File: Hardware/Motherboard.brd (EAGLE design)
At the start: 124.5 x 73.7 mm, 99 parts, among them J1 MICROMOD-2222-C, J10 MICRO-SD-PUSH-PUSH-EXT-PIN, J2 Vertical Qwiic Connector, J4 QWIIC_RIGHT_ANGLE, J5 CORTEX_JTAG_DEBUG_MINIMUM_PTH, J6 MICROMOD_CARRIER, J7 MICROMOD_CARRIER, Q1 3.1A/30V/105mΩ, U2 MCP73831, U5 AP7361C-33

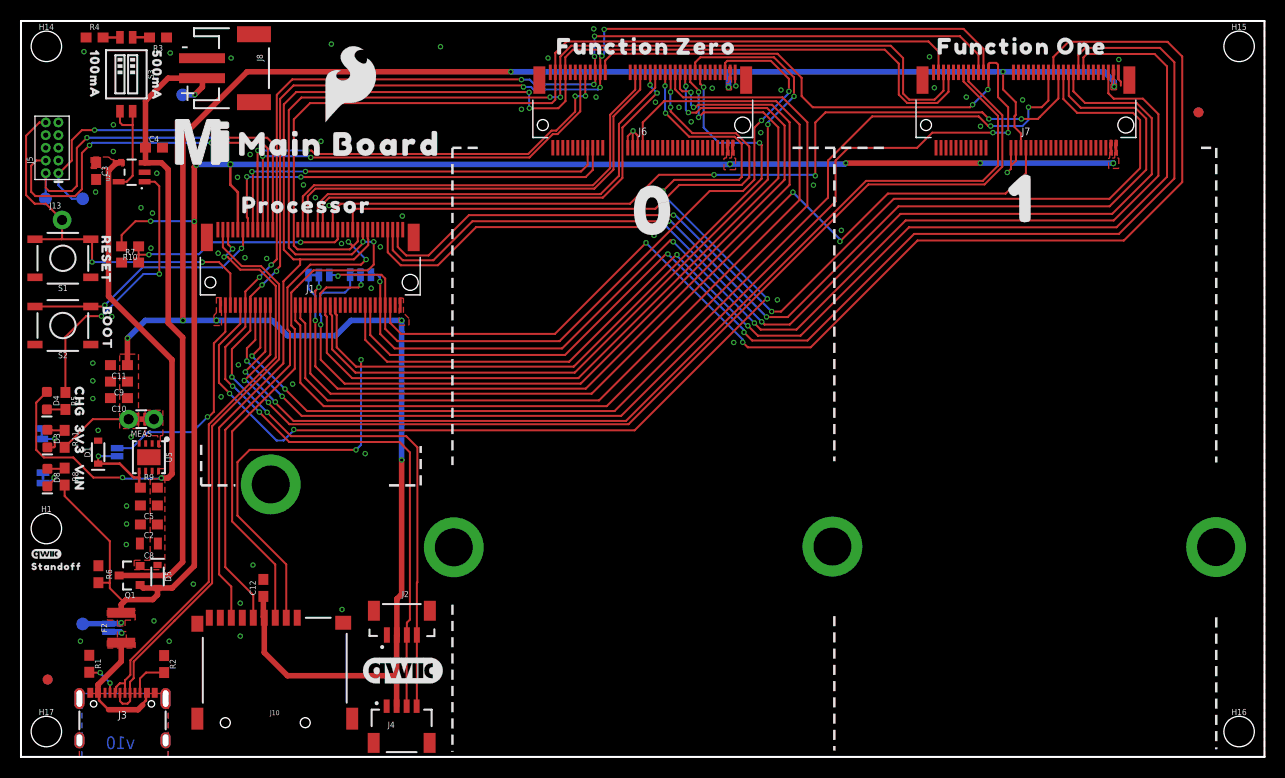
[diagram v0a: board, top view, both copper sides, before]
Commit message: Adds PTH headers for shunt selectable settings on G0 and G1 for PWR_EN0 and PWR_EN1 respectively
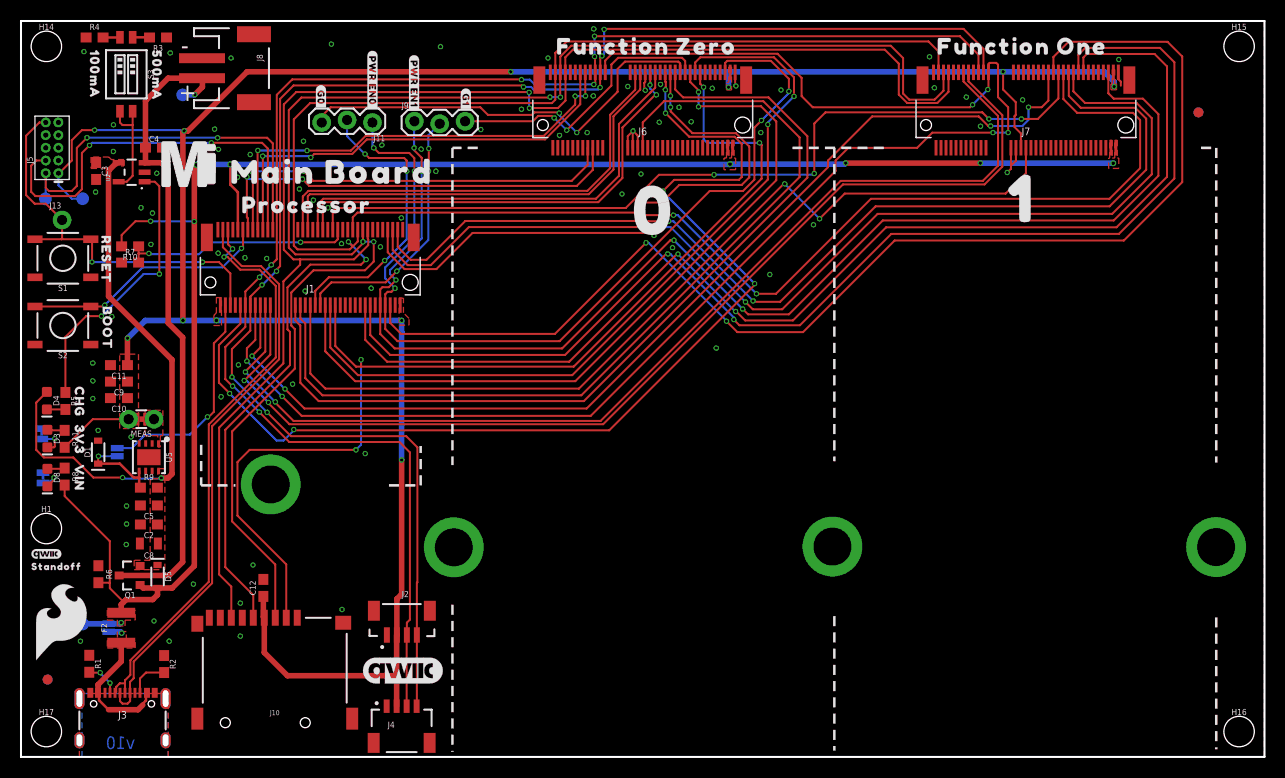
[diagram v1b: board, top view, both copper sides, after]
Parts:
- removed JP1, JP2: JUMPER-SMT_3_1-NC_TRACE_SILK, SparkFun-Jumpers:SMT-JUMPER_3_1-NC_TRACE_SILK
- removed U$28: (no value), top:#ALT_PWR_EN0#517
- added J11, J9: (no value), SparkFun-Connectors:1X03_LOCK
- added U$29: (no value), top:#PWR_EN0#517
- U$25: device top:#G1#PROCESSOR#517 -> top:#PWR_EN1#517
- U$26: device top:#G0#PROCESSOR#517 -> top:#G0#517
- U$27: device top:#ALT_PWR_EN1#517 -> top:#G1#517
- moved U$24 61.1 mm to (4.06, 13.5)
- moved U$25 25.3 mm to (39.3, 67.4), flipped to the top, turned to 270 degrees
- moved U$27 24.4 mm to (44.5, 65.8), flipped to the top, turned to 270 degrees
- moved U$26 23.4 mm to (30.0, 66.0), flipped to the top, turned to 270 degrees
- moved U$21 2.90 mm to (31.1, 58.5)
- moved U$14 2.61 mm to (16.8, 59.4)
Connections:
- net G0-JUMPER: now also J11.2; no longer JP2.2
- net G0-PROCESSOR: now also J11.3; no longer JP2.3
- net G1-JUMPER: now also J9.2; no longer JP1.2
- net G1-PROCESSOR: now also J9.3; no longer JP1.3
- net PWR_EN0: now also J11.1; no longer JP2.1
- net PWR_EN1: now also J9.1; no longer JP1.1
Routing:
- net G1-PROCESSOR: track 87.1 -> 28.4 mm, vias 3 -> 2
- net G0-PROCESSOR: track 87.9 -> 43.5 mm, vias 3 -> 2
- net G0-JUMPER: track 3.16 -> 29.2 mm, vias 1 -> 3
- net G1-JUMPER: track 6.64 -> 26.3 mm, vias 1 -> 3
- net PWR_EN1: track 113.9 -> 130.1 mm, vias 3 -> 5
- net PWR_EN0: track 74.7 -> 90.3 mm, vias 3 -> 5
- net PWM0-PROCESSOR: track 92.7 -> 89.8 mm
- net D0-PROCESSOR: track 111.8 -> 109.3 mm
- net A0-PROCESSOR: track 93.9 -> 91.3 mm
- net D1-PROCESSOR: track 106.9 -> 104.9 mm
- net GND: track 13.0 -> 14.8 mm, vias 73 -> 86
- net I2C_!INT!: track 153.2 -> 151.5 mm
- net A1-PROCESSOR: track 95.2 -> 93.5 mm
- net !CS1!-PROCESSOR: track 124.9 -> 123.5 mm
- net G8-PROCESSOR: track 122.8 -> 121.5 mm
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
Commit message: Revert "Adds PTH headers for shunt selectable settings on G0 and G1 for PWR_EN0 and PWR_EN1 respectively"
This reverts commit ddf80de5a278d55282677fb1bccc97569ea5aff3.
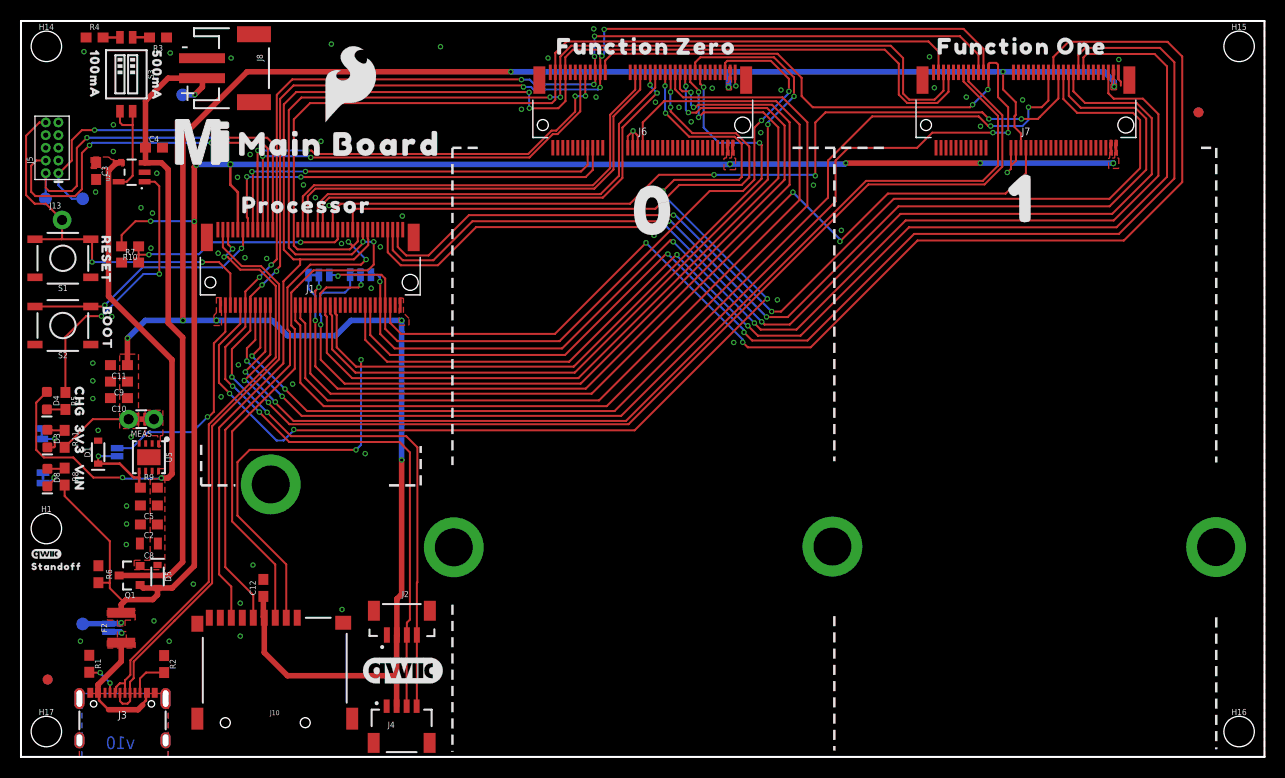
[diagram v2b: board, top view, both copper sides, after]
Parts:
- removed J11, J9: (no value), SparkFun-Connectors:1X03_LOCK
- removed U$29: (no value), top:#PWR_EN0#517
- added JP1, JP2: JUMPER-SMT_3_1-NC_TRACE_SILK, SparkFun-Jumpers:SMT-JUMPER_3_1-NC_TRACE_SILK
- added U$28: (no value), top:#ALT_PWR_EN0#517
- U$25: device top:#PWR_EN1#517 -> top:#G1#PROCESSOR#517
- U$26: device top:#G0#517 -> top:#G0#PROCESSOR#517
- U$27: device top:#G1#517 -> top:#ALT_PWR_EN1#517
- moved U$24 61.1 mm to (33.0, 67.3)
- moved U$25 25.3 mm to (33.4, 42.8), flipped to the bottom, turned to 90 degrees
- moved U$27 24.4 mm to (34.7, 43.4), flipped to the bottom, turned to 90 degrees
- moved U$26 23.4 mm to (29.2, 42.6), flipped to the bottom, turned to 90 degrees
- moved U$21 2.90 mm to (31.9, 61.3)
- moved U$14 2.61 mm to (18.2, 61.6)
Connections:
- net G0-JUMPER: now also JP2.2; no longer J11.2
- net G0-PROCESSOR: now also JP2.3; no longer J11.3
- net G1-JUMPER: now also JP1.2; no longer J9.2
- net G1-PROCESSOR: now also JP1.3; no longer J9.3
- net PWR_EN0: now also JP2.1; no longer J11.1
- net PWR_EN1: now also JP1.1; no longer J9.1
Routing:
- net G1-PROCESSOR: track 28.4 -> 87.1 mm, vias 2 -> 3
- net G0-PROCESSOR: track 43.5 -> 87.9 mm, vias 2 -> 3
- net G0-JUMPER: track 29.2 -> 3.16 mm, vias 3 -> 1
- net G1-JUMPER: track 26.3 -> 6.64 mm, vias 3 -> 1
- net PWR_EN1: track 130.1 -> 113.9 mm, vias 5 -> 3
- net PWR_EN0: track 90.3 -> 74.7 mm, vias 5 -> 3
- net PWM0-PROCESSOR: track 89.8 -> 92.7 mm
- net D0-PROCESSOR: track 109.3 -> 111.8 mm
- net A0-PROCESSOR: track 91.3 -> 93.9 mm
- net D1-PROCESSOR: track 104.9 -> 106.9 mm
- net GND: track 14.8 -> 13.0 mm, vias 86 -> 73
- net I2C_!INT!: track 151.5 -> 153.2 mm
- net A1-PROCESSOR: track 93.5 -> 95.2 mm
- net !CS1!-PROCESSOR: track 123.5 -> 124.9 mm
- net G8-PROCESSOR: track 121.5 -> 122.8 mm
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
